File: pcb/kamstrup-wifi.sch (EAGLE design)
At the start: 2 parts

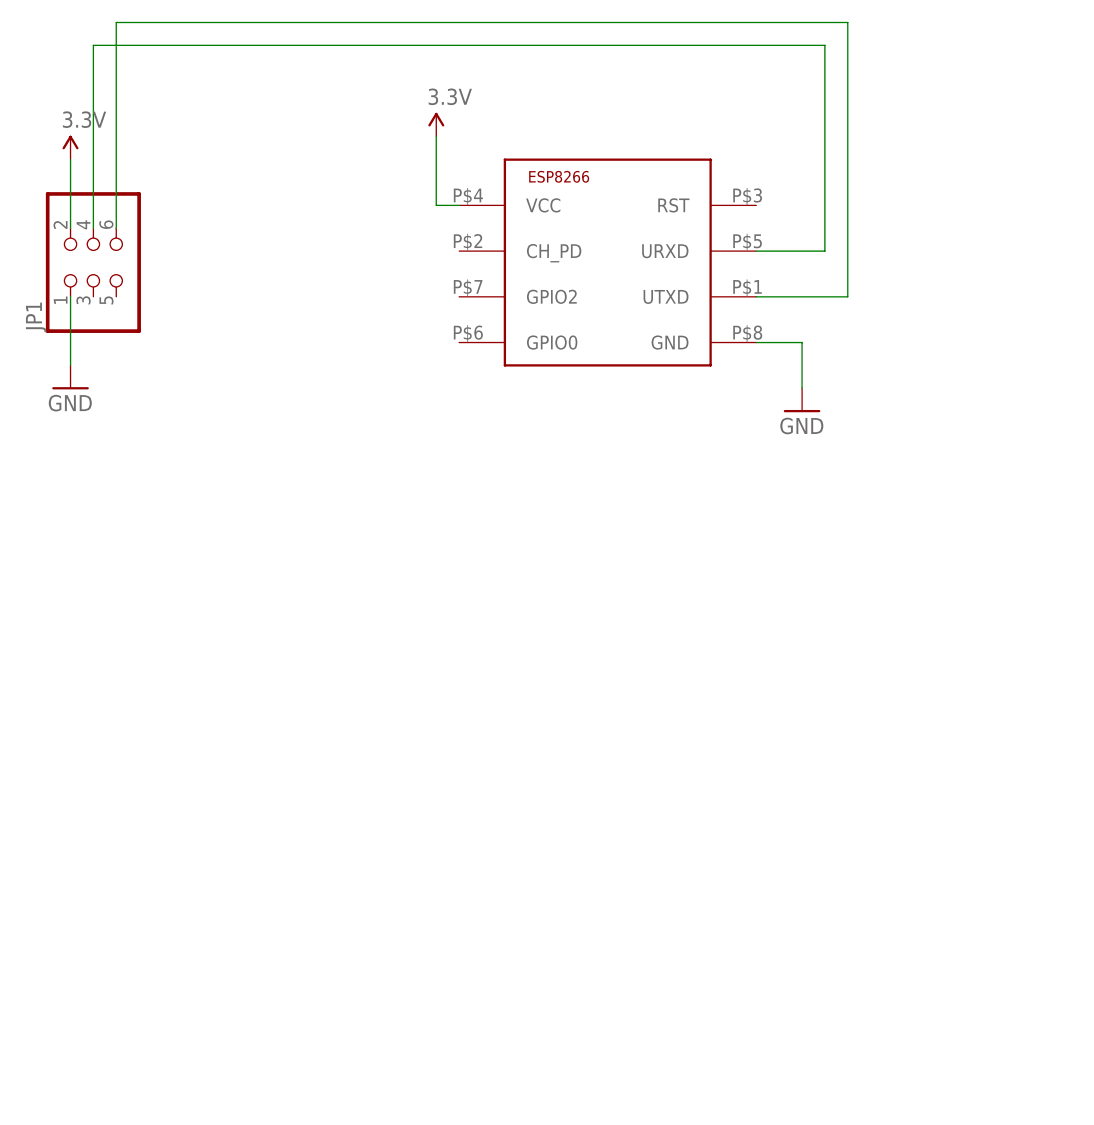
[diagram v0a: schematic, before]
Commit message: pcb: routing done
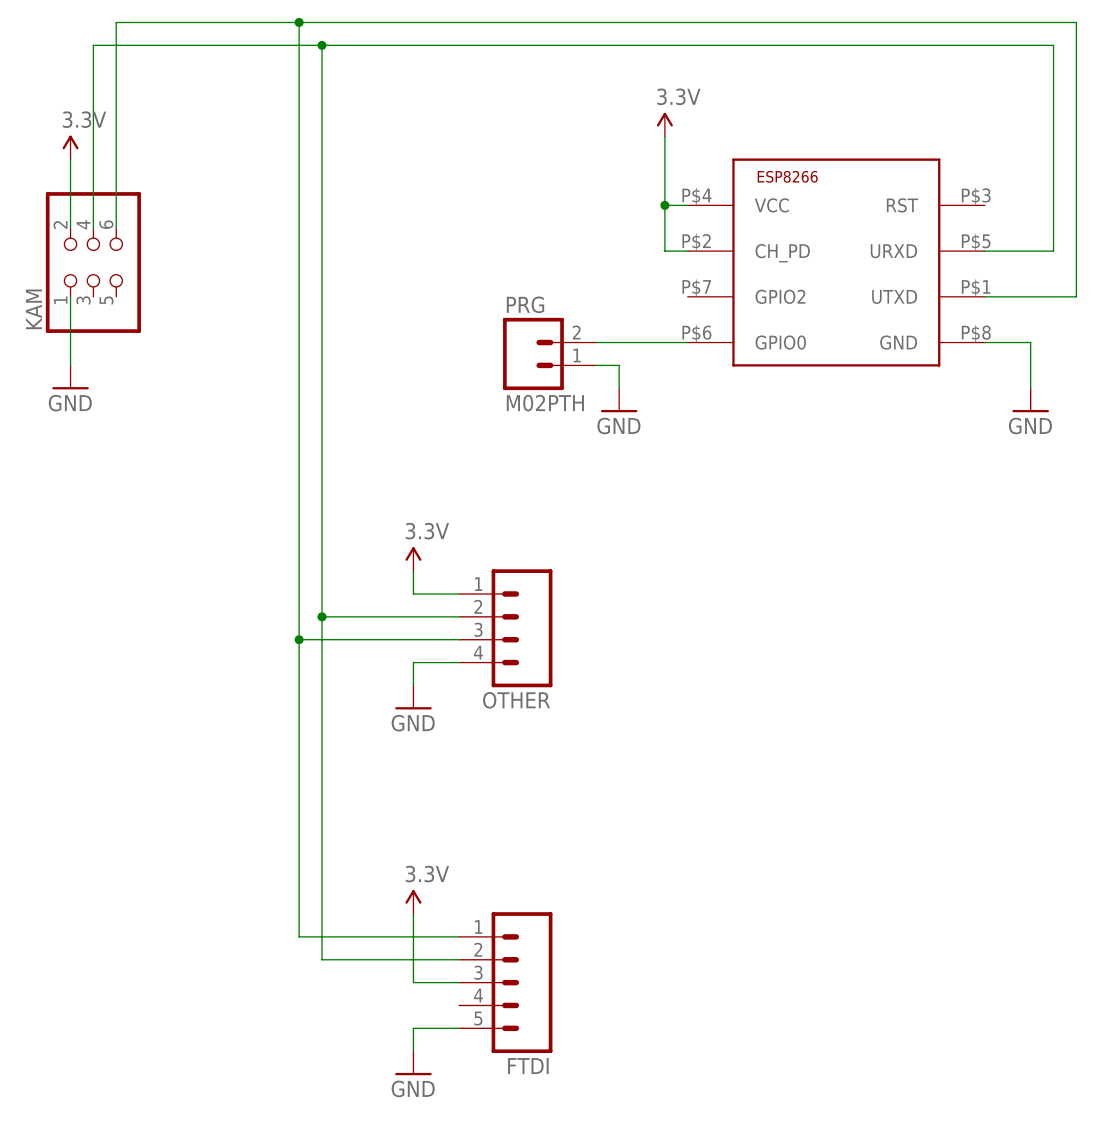
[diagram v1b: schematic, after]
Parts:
- added FTDI: (no value), SparkFun-Connectors:M05PTH
- added OTHER: (no value), SparkFun-Connectors:M04PTH
- added PRG: M02PTH, SparkFun-Connectors:M02PTH
- renumbered JP1 to KAM
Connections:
- new net N$3: PRG.2, U$1.GPIO0
- net 3.3V: now also FTDI.3, OTHER.1, U$1.CH_PD
- net GND: now also FTDI.5, OTHER.4, PRG.1
- net N$1: now also FTDI.1, OTHER.3
- net N$2: now also FTDI.2, OTHER.2
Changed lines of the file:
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@@
 </classes>
 <parts>
-<part name="JP1" library="SparkFun-Connectors" deviceset="PINHD-2X3" device=""/>
+<part name="KAM" library="SparkFun-Connectors" deviceset="PINHD-2X3" device=""/>
 <part name="U$1" library="ESP8266" deviceset="ESP8266-01" device=""/>
 <part name="GND1" library="SparkFun-Aesthetics" deviceset="GND" device=""/>
@@
 <part name="SUPPLY1" library="SparkFun-Aesthetics" deviceset="3.3V" device=""/>
 <part name="SUPPLY2" library="SparkFun-Aesthetics" deviceset="3.3V" device=""/>
+<part name="OTHER" library="SparkFun-Connectors" deviceset="M04" device="PTH"/>
+<part name="GND3" library="SparkFun-Aesthetics" deviceset="GND" device=""/>
+<part name="SUPPLY3" library="SparkFun-Aesthetics" deviceset="3.3V" device=""/>
+<part name="FTDI" library="SparkFun-Connectors" deviceset="M05" device="PTH"/>
+<part name="GND4" library="SparkFun-Aesthetics" deviceset="GND" device=""/>
+<part name="SUPPLY4" library="SparkFun-Aesthetics" deviceset="3.3V" device=""/>
+<part name="PRG" library="SparkFun-Connectors" deviceset="M02" device="PTH"/>
+<part name="GND5" library="SparkFun-Aesthetics" deviceset="GND" device=""/>
 </parts>
 <sheets>
@@
 </plain>
 <instances>
-<instance part="JP1" gate="A" x="15.24" y="63.5" rot="R90"/>
-<instance part="U$1" gate="G$1" x="55.88" y="55.88"/>
+<instance part="KAM" gate="A" x="15.24" y="63.5" rot="R90"/>
+<instance part="U$1" gate="G$1" x="81.28" y="55.88"/>
 <instance part="GND1" gate="1" x="12.7" y="50.8"/>
-<instance part="GND2" gate="1" x="93.98" y="48.26"/>
+<instance part="GND2" gate="1" x="119.38" y="48.26"/>
 <instance part="SUPPLY1" gate="G$1" x="12.7" y="76.2"/>
-<instance part="SUPPLY2" gate="G$1" x="53.34" y="78.74"/>
+<instance part="SUPPLY2" gate="G$1" x="78.74" y="78.74"/>
+<instance part="OTHER" gate="G$1" x="60.96" y="25.4" smashed="yes" rot="R180">
+<attribute name="VALUE" x="66.04" y="33.02" size="1.778" layer="96" rot="R180"/>
+<attribute name="NAME" x="66.04" y="17.018" size="1.778" layer="95" rot="R180"/>
+</instance>
+<instance part="GND3" gate="1" x="50.8" y="15.24"/>
+<instance part="SUPPLY3" gate="G$1" x="50.8" y="30.48"/>
+<instance part="FTDI" gate="G$1" x="63.5" y="-15.24" rot="R180"/>
+<instance part="GND4" gate="1" x="50.8" y="-25.4"/>
+<instance part="SUPPLY4" gate="G$1" x="50.8" y="-7.62"/>
+<instance part="PRG" gate="G$1" x="63.5" y="53.34" smashed="yes">
+<attribute name="VALUE" x="60.96" y="48.26" size="1.778" layer="96"/>
+<attribute name="NAME" x="60.96" y="59.182" size="1.778" layer="95"/>
+</instance>
+<instance part="GND5" gate="1" x="73.66" y="48.26"/>
 </instances>
 <busses>
@@
 <net name="GND" class="0">
 <segment>
-<pinref part="JP1" gate="A" pin="1"/>
+<pinref part="KAM" gate="A" pin="1"/>
 <pinref part="GND1" gate="1" pin="GND"/>
 <wire x1="12.7" y1="60.96" x2="12.7" y2="53.34" width="0.1524" layer="91"/>
@@
 <segment>
 <pinref part="GND2" gate="1" pin="GND"/>
-<wire x1="93.98" y1="50.8" x2="93.98" y2="55.88" width="0.1524" layer="91"/>
+<wire x1="119.38" y1="50.8" x2="119.38" y2="55.88" width="0.1524" layer="91"/>
 <pinref part="U$1" gate="G$1" pin="GND"/>
-<wire x1="93.98" y1="55.88" x2="88.9" y2="55.88" width="0.1524" layer="91"/>
+<wire x1="119.38" y1="55.88" x2="114.3" y2="55.88" width="0.1524" layer="91"/>
+</segment>
+<segment>
+<pinref part="GND3" gate="1" pin="GND"/>
+<wire x1="50.8" y1="17.78" x2="50.8" y2="20.32" width="0.1524" layer="91"/>
+<pinref part="OTHER" gate="G$1" pin="4"/>
+<wire x1="50.8" y1="20.32" x2="55.88" y2="20.32" width="0.1524" layer="91"/>
+</segment>
+<segment>
+<pinref part="GND4" gate="1" pin="GND"/>
+<wire x1="50.8" y1="-22.86" x2="50.8" y2="-20.32" width="0.1524" layer="91"/>
+<pinref part="FTDI" gate="G$1" pin="5"/>
+<wire x1="50.8" y1="-20.32" x2="55.88" y2="-20.32" width="0.1524" layer="91"/>
+</segment>
+<segment>
+<pinref part="PRG" gate="G$1" pin="1"/>
+<pinref part="GND5" gate="1" pin="GND"/>
+<wire x1="71.12" y1="53.34" x2="73.66" y2="53.34" width="0.1524" layer="91"/>
+<wire x1="73.66" y1="53.34" x2="73.66" y2="50.8" width="0.1524" layer="91"/>
 </segment>
 </net>
 <net name="3.3V" class="0">
 <segment>
-<pinref part="JP1" gate="A" pin="2"/>
+<pinref part="KAM" gate="A" pin="2"/>
 <pinref part="SUPPLY1" gate="G$1" pin="3.3V"/>
 <wire x1="12.7" y1="68.58" x2="12.7" y2="76.2" width="0.1524" layer="91"/>
@@
 <segment>
 <pinref part="SUPPLY2" gate="G$1" pin="3.3V"/>
-<wire x1="53.34" y1="78.74" x2="53.34" y2="71.12" width="0.1524" layer="91"/>
+<wire x1="78.74" y1="78.74" x2="78.74" y2="71.12" width="0.1524" layer="91"/>
 <pinref part="U$1" gate="G$1" pin="VCC"/>
-<wire x1="53.34" y1="71.12" x2="55.88" y2="71.12" width="0.1524" layer="91"/>
+<wire x1="78.74" y1="71.12" x2="81.28" y2="71.12" width="0.1524" layer="91"/>
+<pinref part="U$1" gate="G$1" pin="CH_PD"/>
+<wire x1="81.28" y1="66.04" x2="78.74" y2="66.04" width="0.1524" layer="91"/>
+<wire x1="78.74" y1="66.04" x2="78.74" y2="71.12" width="0.1524" layer="91"/>
+<junction x="78.74" y="71.12"/>
+</segment>
+<segment>
+<pinref part="OTHER" gate="G$1" pin="1"/>
+<pinref part="SUPPLY3" gate="G$1" pin="3.3V"/>
+<wire x1="55.88" y1="27.94" x2="50.8" y2="27.94" width="0.1524" layer="91"/>
+<wire x1="50.8" y1="27.94" x2="50.8" y2="30.48" width="0.1524" layer="91"/>
+</segment>
+<segment>
+<pinref part="SUPPLY4" gate="G$1" pin="3.3V"/>
+<wire x1="50.8" y1="-7.62" x2="50.8" y2="-15.24" width="0.1524" layer="91"/>
+<pinref part="FTDI" gate="G$1" pin="3"/>
+<wire x1="50.8" y1="-15.24" x2="55.88" y2="-15.24" width="0.1524" layer="91"/>
 </segment>
 </net>
@@
 <segment>
 <pinref part="U$1" gate="G$1" pin="UTXD"/>
-<wire x1="88.9" y1="60.96" x2="99.06" y2="60.96" width="0.1524" layer="91"/>
-<wire x1="99.06" y1="60.96" x2="99.06" y2="91.44" width="0.1524" layer="91"/>
-<pinref part="JP1" gate="A" pin="6"/>
-<wire x1="99.06" y1="91.44" x2="17.78" y2="91.44" width="0.1524" layer="91"/>
+<wire x1="114.3" y1="60.96" x2="124.46" y2="60.96" width="0.1524" layer="91"/>
+<wire x1="124.46" y1="60.96" x2="124.46" y2="91.44" width="0.1524" layer="91"/>
+<pinref part="KAM" gate="A" pin="6"/>
+<wire x1="124.46" y1="91.44" x2="38.1" y2="91.44" width="0.1524" layer="91"/>
+<wire x1="38.1" y1="91.44" x2="17.78" y2="91.44" width="0.1524" layer="91"/>
 <wire x1="17.78" y1="91.44" x2="17.78" y2="68.58" width="0.1524" layer="91"/>
+<pinref part="OTHER" gate="G$1" pin="3"/>
+<wire x1="55.88" y1="22.86" x2="38.1" y2="22.86" width="0.1524" layer="91"/>
+<wire x1="38.1" y1="22.86" x2="38.1" y2="91.44" width="0.1524" layer="91"/>
+<junction x="38.1" y="91.44"/>
+<pinref part="FTDI" gate="G$1" pin="1"/>
+<wire x1="55.88" y1="-10.16" x2="38.1" y2="-10.16" width="0.1524" layer="91"/>
+<wire x1="38.1" y1="-10.16" x2="38.1" y2="22.86" width="0.1524" layer="91"/>
+<junction x="38.1" y="22.86"/>
 </segment>
 </net>
 <net name="N$2" class="0">
 <segment>
-<pinref part="JP1" gate="A" pin="4"/>
+<pinref part="KAM" gate="A" pin="4"/>
 <wire x1="15.24" y1="68.58" x2="15.24" y2="88.9" width="0.1524" layer="91"/>
-<wire x1="15.24" y1="88.9" x2="96.52" y2="88.9" width="0.1524" layer="91"/>
-<wire x1="96.52" y1="88.9" x2="96.52" y2="66.04" width="0.1524" layer="91"/>
+<wire x1="15.24" y1="88.9" x2="40.64" y2="88.9" width="0.1524" layer="91"/>
+<wire x1="40.64" y1="88.9" x2="121.92" y2="88.9" width="0.1524" layer="91"/>
+<wire x1="121.92" y1="88.9" x2="121.92" y2="66.04" width="0.1524" layer="91"/>
 <pinref part="U$1" gate="G$1" pin="URXD"/>
-<wire x1="96.52" y1="66.04" x2="88.9" y2="66.04" width="0.1524" layer="91"/>
+<wire x1="121.92" y1="66.04" x2="114.3" y2="66.04" width="0.1524" layer="91"/>
+<pinref part="OTHER" gate="G$1" pin="2"/>
+<wire x1="55.88" y1="25.4" x2="40.64" y2="25.4" width="0.1524" layer="91"/>
+<wire x1="40.64" y1="25.4" x2="40.64" y2="88.9" width="0.1524" layer="91"/>
+<junction x="40.64" y="88.9"/>
+<pinref part="FTDI" gate="G$1" pin="2"/>
+<wire x1="55.88" y1="-12.7" x2="40.64" y2="-12.7" width="0.1524" layer="91"/>
+<wire x1="40.64" y1="-12.7" x2="40.64" y2="25.4" width="0.1524" layer="91"/>
+<junction x="40.64" y="25.4"/>
 </segment>
 </net>
+<net name="N$3" class="0">
+<segment>
+<pinref part="PRG" gate="G$1" pin="2"/>
+<pinref part="U$1" gate="G$1" pin="GPIO0"/>
+<wire x1="71.12" y1="55.88" x2="81.28" y2="55.88" width="0.1524" layer="91"/>
+</segment>
+</net>

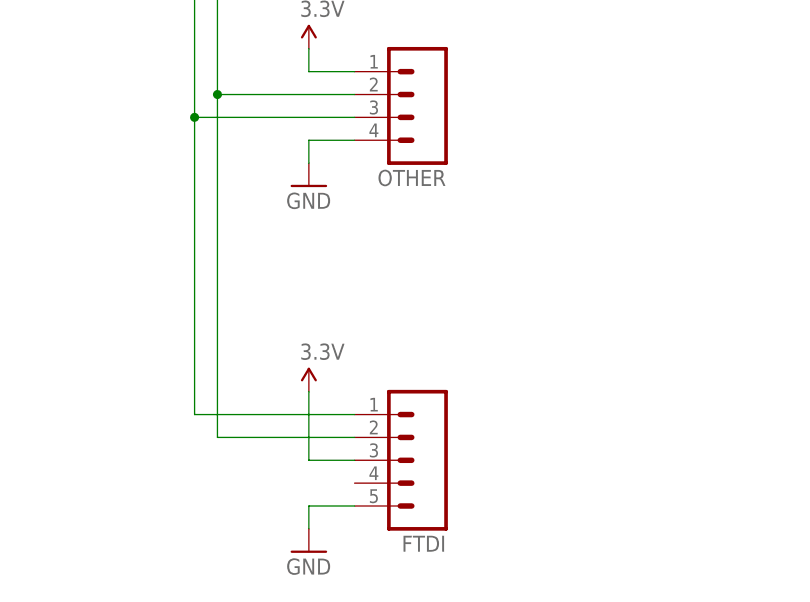
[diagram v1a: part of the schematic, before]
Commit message: pcb: + silk and no cupper under antenna
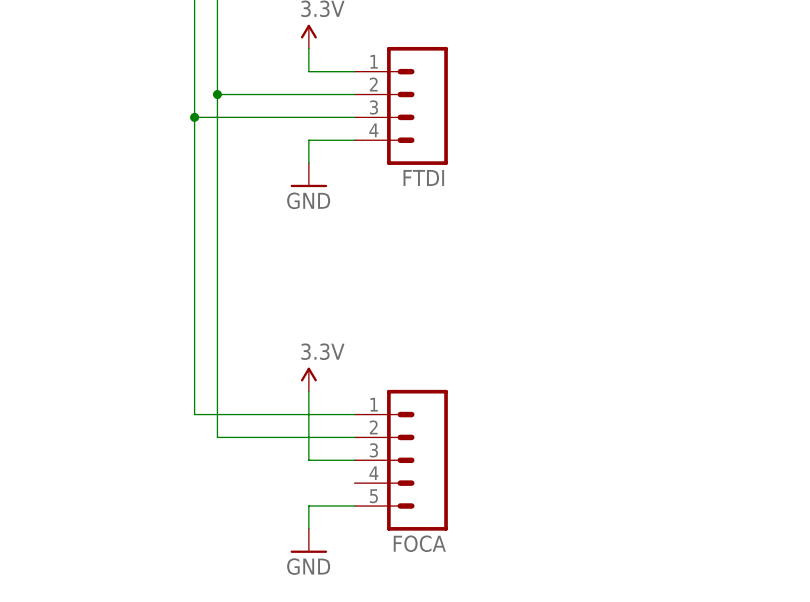
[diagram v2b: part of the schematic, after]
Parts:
- removed OTHER: (no value), SparkFun-Connectors:M04PTH
- added FOCA: (no value), SparkFun-Connectors:M05PTH
- FTDI: device SparkFun-Connectors:M05PTH -> SparkFun-Connectors:M04PTH
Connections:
- net 3.3V: now also FOCA.3, FTDI.1; no longer FTDI.3, OTHER.1
- net GND: now also FOCA.5, FTDI.4; no longer FTDI.5, OTHER.4
- net N$1: now also FOCA.1, FTDI.3; no longer FTDI.1, OTHER.3
- net N$2: now also FOCA.2; no longer OTHER.2
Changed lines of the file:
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@@
 <part name="SUPPLY1" library="SparkFun-Aesthetics" deviceset="3.3V" device=""/>
 <part name="SUPPLY2" library="SparkFun-Aesthetics" deviceset="3.3V" device=""/>
-<part name="OTHER" library="SparkFun-Connectors" deviceset="M04" device="PTH"/>
+<part name="FTDI" library="SparkFun-Connectors" deviceset="M04" device="PTH"/>
 <part name="GND3" library="SparkFun-Aesthetics" deviceset="GND" device=""/>
 <part name="SUPPLY3" library="SparkFun-Aesthetics" deviceset="3.3V" device=""/>
-<part name="FTDI" library="SparkFun-Connectors" deviceset="M05" device="PTH"/>
+<part name="FOCA" library="SparkFun-Connectors" deviceset="M05" device="PTH"/>
 <part name="GND4" library="SparkFun-Aesthetics" deviceset="GND" device=""/>
 <part name="SUPPLY4" library="SparkFun-Aesthetics" deviceset="3.3V" device=""/>
@@
 <instance part="SUPPLY1" gate="G$1" x="12.7" y="76.2"/>
 <instance part="SUPPLY2" gate="G$1" x="78.74" y="78.74"/>
-<instance part="OTHER" gate="G$1" x="60.96" y="25.4" smashed="yes" rot="R180">
+<instance part="FTDI" gate="G$1" x="60.96" y="25.4" smashed="yes" rot="R180">
 <attribute name="VALUE" x="66.04" y="33.02" size="1.778" layer="96" rot="R180"/>
 <attribute name="NAME" x="66.04" y="17.018" size="1.778" layer="95" rot="R180"/>
@@
 <instance part="GND3" gate="1" x="50.8" y="15.24"/>
 <instance part="SUPPLY3" gate="G$1" x="50.8" y="30.48"/>
-<instance part="FTDI" gate="G$1" x="63.5" y="-15.24" rot="R180"/>
+<instance part="FOCA" gate="G$1" x="63.5" y="-15.24" rot="R180"/>
 <instance part="GND4" gate="1" x="50.8" y="-25.4"/>
 <instance part="SUPPLY4" gate="G$1" x="50.8" y="-7.62"/>
@@
 <pinref part="GND3" gate="1" pin="GND"/>
 <wire x1="50.8" y1="17.78" x2="50.8" y2="20.32" width="0.1524" layer="91"/>
-<pinref part="OTHER" gate="G$1" pin="4"/>
+<pinref part="FTDI" gate="G$1" pin="4"/>
 <wire x1="50.8" y1="20.32" x2="55.88" y2="20.32" width="0.1524" layer="91"/>
 </segment>
@@
 <pinref part="GND4" gate="1" pin="GND"/>
 <wire x1="50.8" y1="-22.86" x2="50.8" y2="-20.32" width="0.1524" layer="91"/>
-<pinref part="FTDI" gate="G$1" pin="5"/>
+<pinref part="FOCA" gate="G$1" pin="5"/>
 <wire x1="50.8" y1="-20.32" x2="55.88" y2="-20.32" width="0.1524" layer="91"/>
 </segment>
@@
 </segment>
 <segment>
-<pinref part="OTHER" gate="G$1" pin="1"/>
+<pinref part="FTDI" gate="G$1" pin="1"/>
 <pinref part="SUPPLY3" gate="G$1" pin="3.3V"/>
 <wire x1="55.88" y1="27.94" x2="50.8" y2="27.94" width="0.1524" layer="91"/>
@@
 <pinref part="SUPPLY4" gate="G$1" pin="3.3V"/>
 <wire x1="50.8" y1="-7.62" x2="50.8" y2="-15.24" width="0.1524" layer="91"/>
-<pinref part="FTDI" gate="G$1" pin="3"/>
+<pinref part="FOCA" gate="G$1" pin="3"/>
 <wire x1="50.8" y1="-15.24" x2="55.88" y2="-15.24" width="0.1524" layer="91"/>
 </segment>
@@
 <wire x1="38.1" y1="91.44" x2="17.78" y2="91.44" width="0.1524" layer="91"/>
 <wire x1="17.78" y1="91.44" x2="17.78" y2="68.58" width="0.1524" layer="91"/>
-<pinref part="OTHER" gate="G$1" pin="3"/>
+<pinref part="FTDI" gate="G$1" pin="3"/>
 <wire x1="55.88" y1="22.86" x2="38.1" y2="22.86" width="0.1524" layer="91"/>
 <wire x1="38.1" y1="22.86" x2="38.1" y2="91.44" width="0.1524" layer="91"/>
 <junction x="38.1" y="91.44"/>
-<pinref part="FTDI" gate="G$1" pin="1"/>
+<pinref part="FOCA" gate="G$1" pin="1"/>
 <wire x1="55.88" y1="-10.16" x2="38.1" y2="-10.16" width="0.1524" layer="91"/>
 <wire x1="38.1" y1="-10.16" x2="38.1" y2="22.86" width="0.1524" layer="91"/>
@@
 <pinref part="U$1" gate="G$1" pin="URXD"/>
 <wire x1="121.92" y1="66.04" x2="114.3" y2="66.04" width="0.1524" layer="91"/>
-<pinref part="OTHER" gate="G$1" pin="2"/>
+<pinref part="FTDI" gate="G$1" pin="2"/>
 <wire x1="55.88" y1="25.4" x2="40.64" y2="25.4" width="0.1524" layer="91"/>
 <wire x1="40.64" y1="25.4" x2="40.64" y2="88.9" width="0.1524" layer="91"/>
 <junction x="40.64" y="88.9"/>
-<pinref part="FTDI" gate="G$1" pin="2"/>
+<pinref part="FOCA" gate="G$1" pin="2"/>
 <wire x1="55.88" y1="-12.7" x2="40.64" y2="-12.7" width="0.1524" layer="91"/>
 <wire x1="40.64" y1="-12.7" x2="40.64" y2="25.4" width="0.1524" layer="91"/>
